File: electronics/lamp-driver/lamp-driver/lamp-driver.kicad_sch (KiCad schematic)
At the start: 30 parts, among them J1 Conn_01x04_Pin, J12V1 Conn_01x02_Pin, J2 Conn_01x04_Pin, J3 Conn_01x04_Pin, J4 Conn_01x04_Pin, J5 Conn_01x04_Pin, J6 Conn_01x04_Pin, Q1 AO3400A, U1 LM78M05_TO252

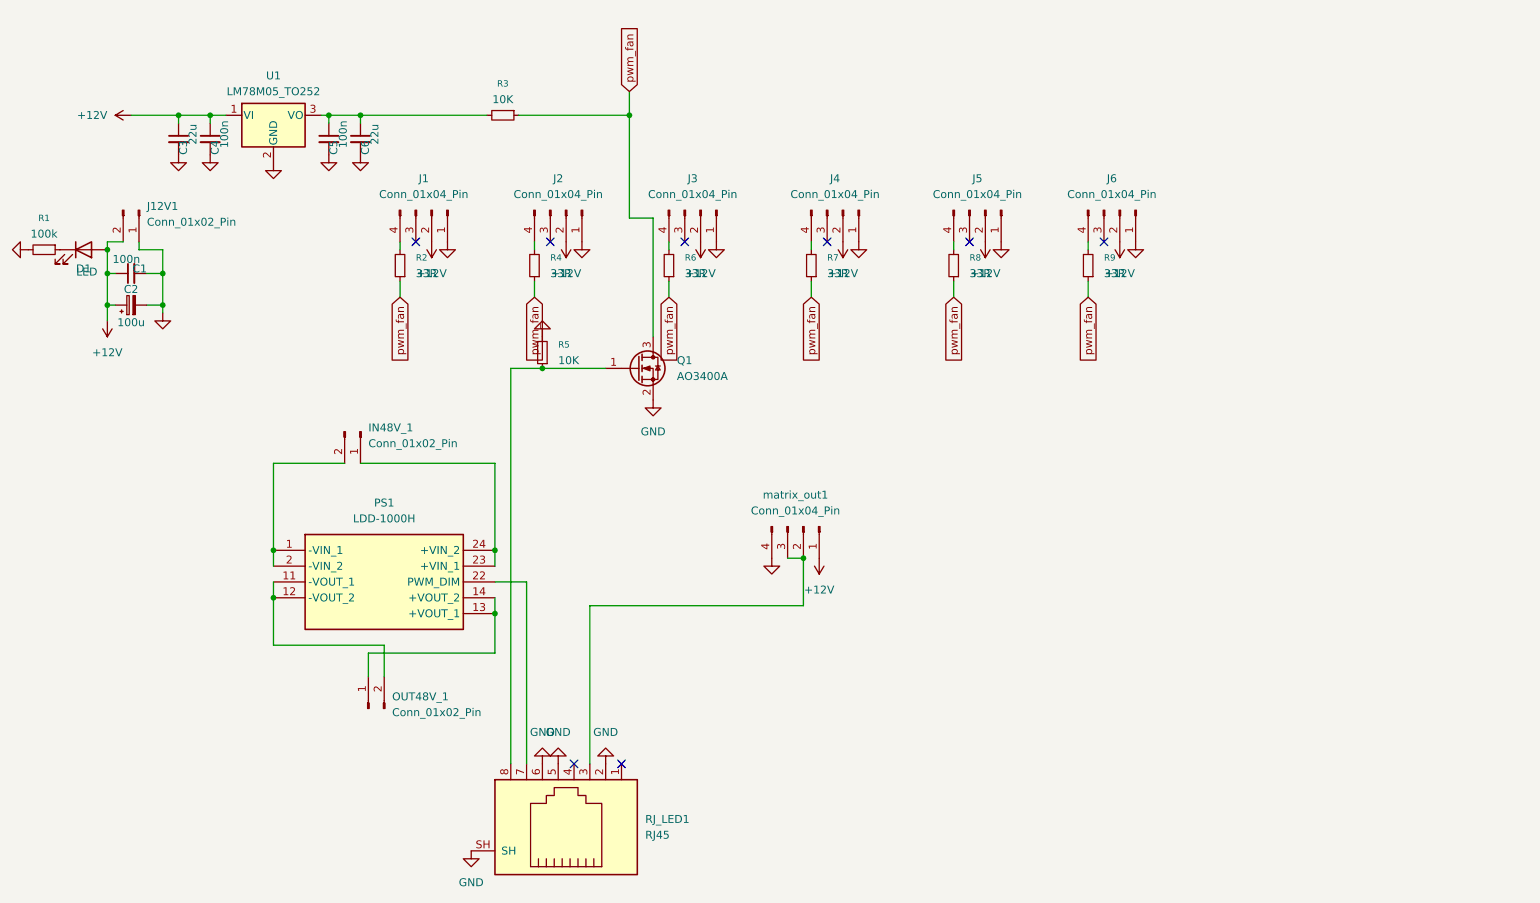
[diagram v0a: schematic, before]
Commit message: lamp fans control added; uv boost anims added; ambiente light timeout fixed
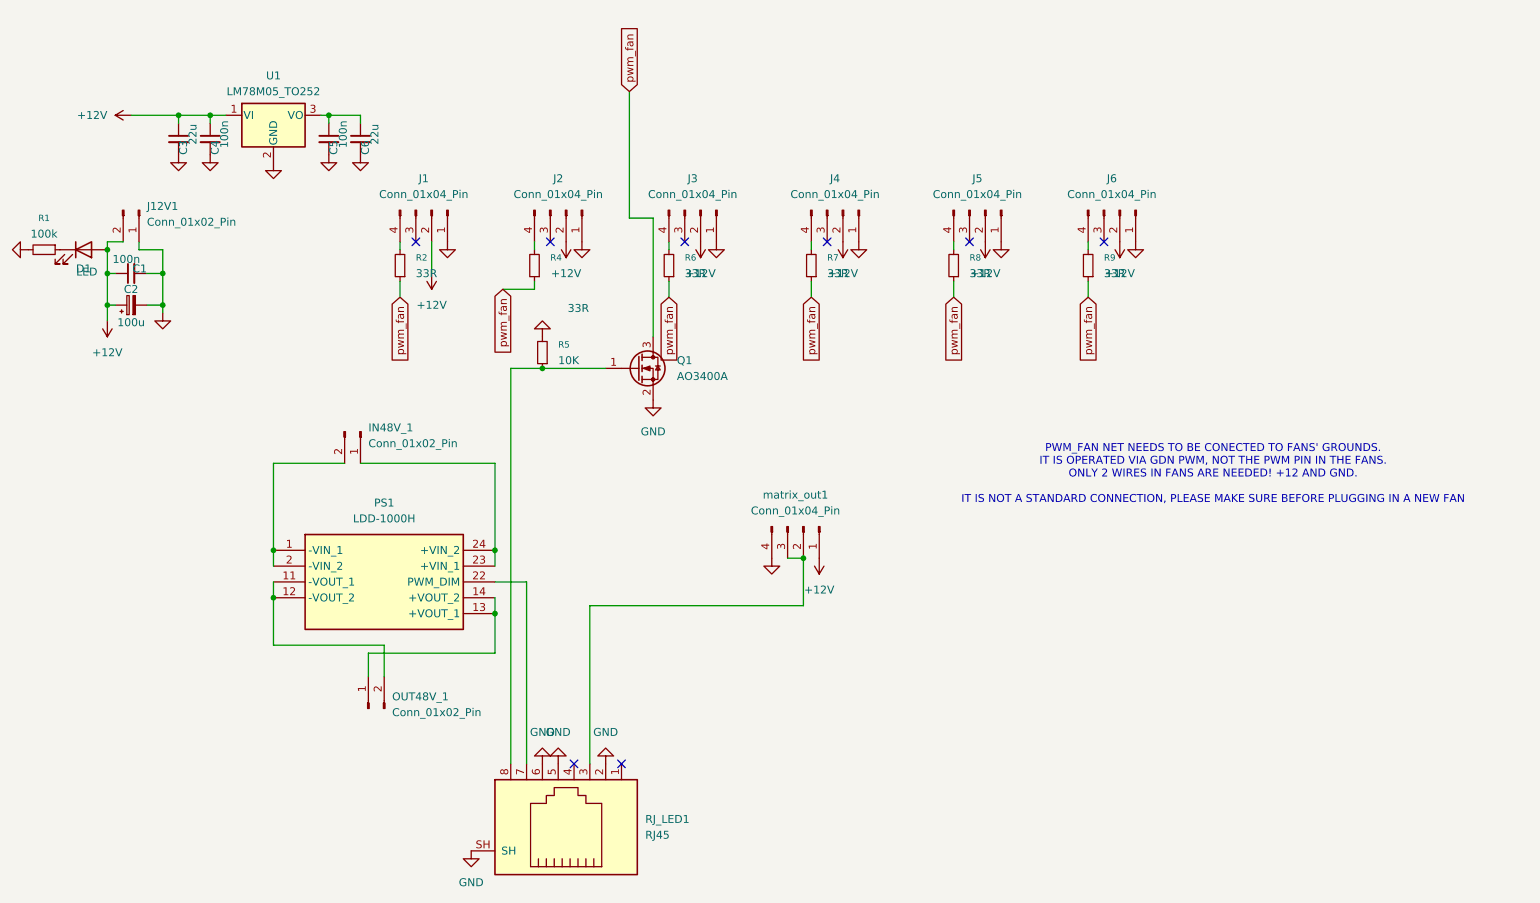
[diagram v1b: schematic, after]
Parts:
- removed R3: 10K, Resistor_SMD:R_0805_2012Metric, symbol Device:R_Small
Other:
- note added: "PWM_FAN NET NEEDS TO BE CONECTED TO FANS' GROUNDS. IT IS OPERATED VIA GDN PWM, NOT THE PWM PIN IN THE FANS. ONLY 2 WIRES IN FANS ARE NEEDED! +12 AND GND. IT IS NOT A STANDARD CONNECTION, PLEASE MAKE SURE BEFORE PLUGGING IN A NEW FAN"
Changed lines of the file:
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@@
 	(generator_version "9.0")
 	(paper "A4")
+	(text "PWM_FAN NET NEEDS TO BE CONECTED TO FANS' GROUNDS. \nIT IS OPERATED VIA GDN PWM, NOT THE PWM PIN IN THE FANS. \nONLY 2 WIRES IN FANS ARE NEEDED! +12 AND GND. \n\nIT IS NOT A STANDARD CONNECTION, PLEASE MAKE SURE BEFORE PLUGGING IN A NEW FAN"
+		(exclude_from_sim no)
+		(at 192.786 74.168 0)
+		(effects
+			(font
+				(size 1.27 1.27)
+			)
+		)
+	)
 	(junction
 		(at 127 87.63)
@@
 	)
 	(junction
-		(at 55.88 16.51)
-		(diameter 0)
-		(color 0 0 0 0)
-	)
-	(junction
 		(at 24.13 46.99)
 		(diameter 0)
@@
 	)
 	(junction
-		(at 99.06 16.51)
-		(diameter 0)
-		(color 0 0 0 0)
-	)
-	(junction
 		(at 24.13 41.91)
 		(diameter 0)
@@
 	(wire
 		(pts
+			(xy 83.82 44.45) (xy 83.82 43.18)
+		)
+		(stroke
+			(width 0)
+			(type default)
+		)
+	)
+	(wire
+		(pts
 			(xy 124.46 87.63) (xy 127 87.63)
 		)
@@
 	(wire
 		(pts
-			(xy 99.06 12.7) (xy 99.06 16.51)
+			(xy 99.06 12.7) (xy 99.06 33.02)
 		)
 		(stroke
@@
 	(wire
 		(pts
-			(xy 81.28 16.51) (xy 99.06 16.51)
+			(xy 128.27 45.72) (xy 128.27 43.18)
 		)
 		(stroke
@@
 	(wire
 		(pts
-			(xy 128.27 45.72) (xy 128.27 43.18)
+			(xy 127 95.25) (xy 127 87.63)
 		)
 		(stroke
@@
 	(wire
 		(pts
-			(xy 127 95.25) (xy 127 87.63)
+			(xy 85.09 57.15) (xy 95.25 57.15)
 		)
 		(stroke
@@
 	(wire
 		(pts
-			(xy 85.09 57.15) (xy 95.25 57.15)
+			(xy 77.47 93.98) (xy 77.47 96.52)
 		)
 		(stroke
@@
 	(wire
 		(pts
-			(xy 77.47 93.98) (xy 77.47 96.52)
+			(xy 151.13 38.1) (xy 151.13 36.83)
 		)
 		(stroke
@@
 	(wire
 		(pts
-			(xy 151.13 38.1) (xy 151.13 36.83)
+			(xy 67.31 41.91) (xy 67.31 36.83)
 		)
 		(stroke
@@
 	(wire
 		(pts
-			(xy 55.88 16.51) (xy 76.2 16.51)
-		)
-		(stroke
-			(width 0)
-			(type default)
-		)
-	)
-	(wire
-		(pts
 			(xy 82.55 91.44) (xy 82.55 120.65)
 		)
@@
 	(wire
 		(pts
-			(xy 99.06 16.51) (xy 99.06 33.02)
-		)
-		(stroke
-			(width 0)
-			(type default)
-		)
-	)
-	(wire
-		(pts
 			(xy 105.41 38.1) (xy 105.41 36.83)
 		)
@@
 	(wire
 		(pts
-			(xy 92.71 95.25) (xy 127 95.25)
+			(xy 78.74 44.45) (xy 83.82 44.45)
 		)
 		(stroke
@@
 	(wire
 		(pts
-			(xy 41.91 101.6) (xy 59.69 101.6)
+			(xy 92.71 95.25) (xy 127 95.25)
 		)
 		(stroke
@@
 	(wire
 		(pts
-			(xy 83.82 45.72) (xy 83.82 43.18)
+			(xy 41.91 101.6) (xy 59.69 101.6)
 		)
 		(stroke
@@
 	(global_label "pwm_fan"
 		(shape input)
-		(at 83.82 45.72 270)
+		(at 78.74 44.45 270)
 		(fields_autoplaced yes)
 		(effects
@@
 		)
 		(property "Intersheetrefs" "${INTERSHEET_REFS}"
-			(at 83.82 56.8693 90)
+			(at 78.74 55.5993 90)
 			(effects
 				(font
@@
 		(on_board yes)
 		(dnp no)
-		(fields_autoplaced yes)
 		(property "Reference" "R4"
 			(at 86.36 39.3699 0)
@@
 		)
 		(property "Value" "33R"
-			(at 86.36 41.9099 0)
+			(at 89.154 47.498 0)
 			(effects
 				(font
@@
 	(symbol
 		(lib_id "power:+12V")
-		(at 67.31 36.83 180)
+		(at 67.31 41.91 180)
 		(unit 1)
 		(exclude_from_sim no)
@@
 		(fields_autoplaced yes)
 		(property "Reference" "#PWR010"
-			(at 67.31 33.02 0)
+			(at 67.31 38.1 0)
 			(effects
 				(font
@@
 		)
 		(property "Value" "+12V"
-			(at 67.31 41.91 0)
+			(at 67.31 46.99 0)
 			(effects
 				(font
@@
 		)
 		(property "Footprint" ""
-			(at 67.31 36.83 0)
+			(at 67.31 41.91 0)
 			(effects
 				(font
@@
 		)
 		(property "Datasheet" ""
-			(at 67.31 36.83 0)
+			(at 67.31 41.91 0)
 			(effects
 				(font
@@
 		)
 		(property "Description" "Power symbol creates a global label with name \"+12V\""
-			(at 67.31 36.83 0)
+			(at 67.31 41.91 0)
 			(effects
 				(font
@@
 					(unit 1)
 				)
-			)
-		)
-	)
-	(symbol
-		(lib_id "Device:R_Small")
-		(at 78.74 16.51 270)
-		(unit 1)
-		(exclude_from_sim no)
-		(in_bom yes)
-		(on_board yes)
-		(dnp no)
-		(fields_autoplaced yes)
-		(property "Reference" "R3"
-			(at 78.74 11.43 90)
-			(effects
-				(font
-					(size 1.016 1.016)
-				)
-			)
-		)
-		(property "Value" "10K"
-			(at 78.74 13.97 90)
-			(effects
-				(font
-					(size 1.27 1.27)
-				)
-			)
-		)
-		(property "Footprint" "Resistor_SMD:R_0805_2012Metric"
-			(at 78.74 16.51 0)
-			(effects
-				(font
-					(size 1.27 1.27)
-				)
-				(hide yes)
-			)
-		)
-		(property "Datasheet" "~"
-			(at 78.74 16.51 0)
-			(effects
-				(font
-					(size 1.27 1.27)
-				)
-				(hide yes)
-			)
-		)
-		(property "Description" "Resistor, small symbol"
-			(at 78.74 16.51 0)
-			(effects
-				(font
-					(size 1.27 1.27)
-				)
-				(hide yes)
-			)
-		)
-		(pin "2"
-		)
-		(pin "1"
-		)
-		(instances
-			(project "lamp-driver"
-				(path "/8d1b4815-1b67-41e7-a6f2-54ca5c4f4dfa"
-					(reference "R3")
-					(unit 1)
-				)

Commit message: fail safe added to lamp fans
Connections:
- net GND: no longer R5.2
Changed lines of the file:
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@@
-	)
-	(symbol
-		(lib_id "power:GND")
-		(at 85.09 52.07 180)
-		(unit 1)
-		(exclude_from_sim no)
-		(in_bom yes)
-		(on_board yes)
-		(dnp no)
-		(fields_autoplaced yes)
-		(property "Reference" "#PWR012"
-			(at 85.09 45.72 0)
-			(effects
-				(font
-					(size 1.27 1.27)
-				)
-				(hide yes)
-			)
-		)
-		(property "Value" "GND"
-			(at 85.09 46.99 0)
-			(effects
-				(font
-					(size 1.27 1.27)
-				)
-				(hide yes)
-			)
-		)
-		(property "Footprint" ""
-			(at 85.09 52.07 0)
-			(effects
-				(font
-					(size 1.27 1.27)
-				)
-				(hide yes)
-			)
-		)
-		(property "Datasheet" ""
-			(at 85.09 52.07 0)
-			(effects
-				(font
-					(size 1.27 1.27)
-				)
-				(hide yes)
-			)
-		)
-		(property "Description" "Power symbol creates a global label with name \"GND\" , ground"
-			(at 85.09 52.07 0)
-			(effects
-				(font
-					(size 1.27 1.27)
-				)
-				(hide yes)
-			)
-		)
-		(pin "1"
-		)
-		(instances
-			(project "lamp-driver"
-				(path "/8d1b4815-1b67-41e7-a6f2-54ca5c4f4dfa"
-					(reference "#PWR012")
-					(unit 1)
-				)
-			)
-		)
 	)
 	(symbol

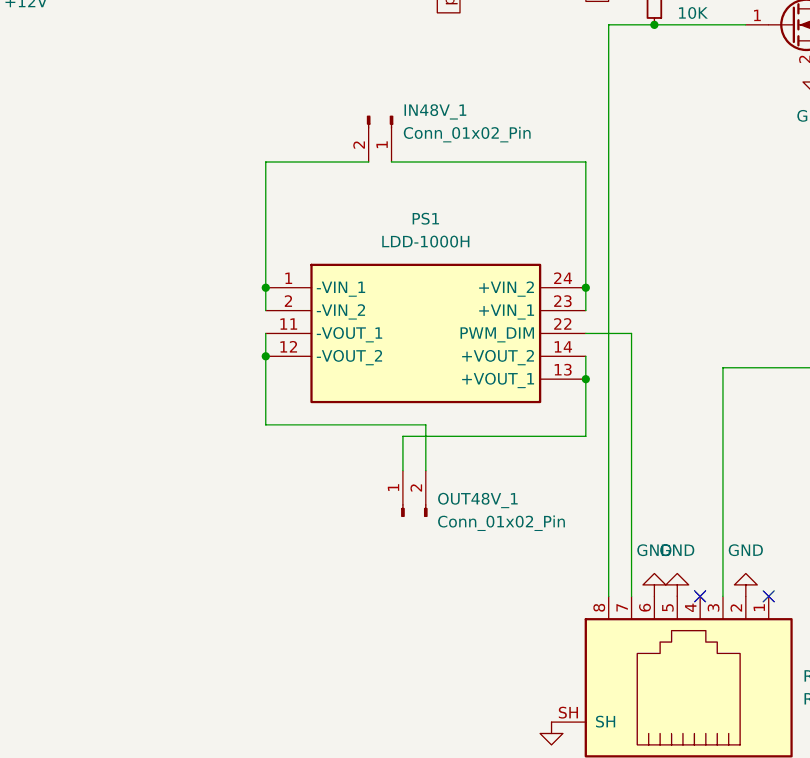
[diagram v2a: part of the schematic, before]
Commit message: UV control fixed
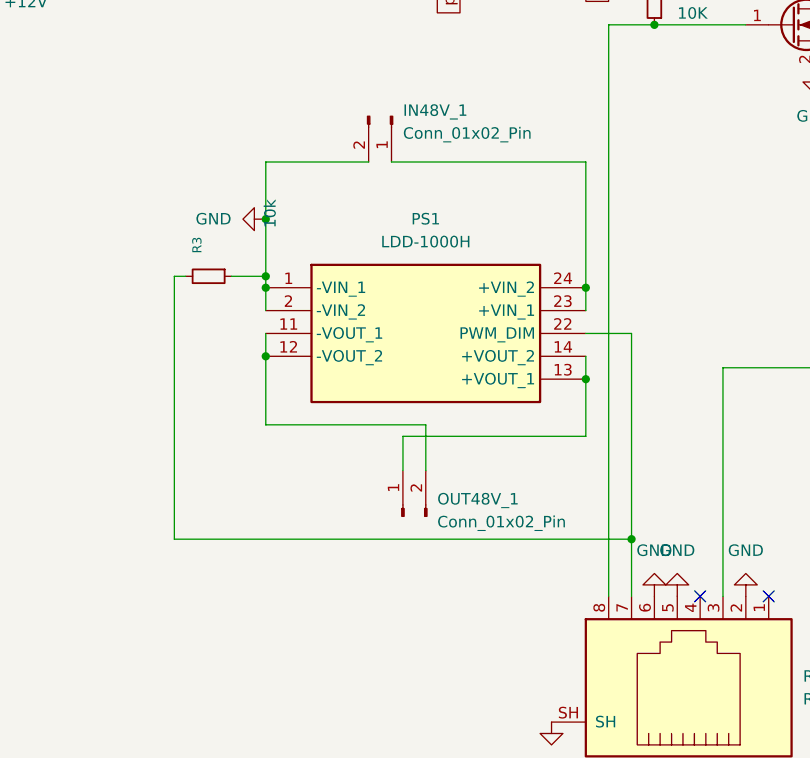
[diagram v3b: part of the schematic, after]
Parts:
- added R3: 10k, Resistor_SMD:R_0805_2012Metric, symbol Device:R_Small
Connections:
- net GND: now also IN48V_1.2 (Pin_2), PS1.1 (-VIN_1), PS1.2 (-VIN_2), R3.1
- net at PS1.22 (PWM_DIM), RJ_LED1.7: now also R3.2
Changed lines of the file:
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@@
 	)
 	(junction
+		(at 41.91 78.74)
+		(diameter 0)
+		(color 0 0 0 0)
+	)
+	(junction
 		(at 15.24 38.1)
 		(diameter 0)
@@
 	)
 	(junction
+		(at 82.55 114.3)
+		(diameter 0)
+		(color 0 0 0 0)
+	)
+	(junction
+		(at 41.91 85.09)
+		(diameter 0)
+		(color 0 0 0 0)
+	)
+	(junction
 		(at 24.13 41.91)
 		(diameter 0)
@@
 	(wire
 		(pts
-			(xy 41.91 72.39) (xy 41.91 86.36)
+			(xy 41.91 72.39) (xy 41.91 78.74)
 		)
 		(stroke
@@
 	(wire
 		(pts
+			(xy 41.91 85.09) (xy 41.91 86.36)
+		)
+		(stroke
+			(width 0)
+			(type default)
+		)
+	)
+	(wire
+		(pts
 			(xy 99.06 12.7) (xy 99.06 33.02)
 		)
@@
 	(wire
 		(pts
+			(xy 31.75 85.09) (xy 33.02 85.09)
+		)
+		(stroke
+			(width 0)
+			(type default)
+		)
+	)
+	(wire
+		(pts
 			(xy 77.47 96.52) (xy 77.47 102.87)
 		)
@@
 	(wire
 		(pts
+			(xy 41.91 78.74) (xy 41.91 85.09)
+		)
+		(stroke
+			(width 0)
+			(type default)
+		)
+	)
+	(wire
+		(pts
 			(xy 128.27 45.72) (xy 128.27 43.18)
 		)
@@
 	(wire
 		(pts
+			(xy 82.55 114.3) (xy 82.55 120.65)
+		)
+		(stroke
+			(width 0)
+			(type default)
+		)
+	)
+	(wire
+		(pts
+			(xy 82.55 114.3) (xy 31.75 114.3)
+		)
+		(stroke
+			(width 0)
+			(type default)
+		)
+	)
+	(wire
+		(pts
 			(xy 55.88 72.39) (xy 77.47 72.39)
 		)
@@
 	(wire
 		(pts
-			(xy 82.55 91.44) (xy 82.55 120.65)
+			(xy 82.55 91.44) (xy 82.55 114.3)
 		)
 		(stroke
@@
 	(wire
 		(pts
+			(xy 31.75 85.09) (xy 31.75 114.3)
+		)
+		(stroke
+			(width 0)
+			(type default)
+		)
+	)
+	(wire
+		(pts
 			(xy 80.01 120.65) (xy 80.01 57.15)
 		)
@@
 	(wire
 		(pts
+			(xy 38.1 85.09) (xy 41.91 85.09)
+		)
+		(stroke
+			(width 0)
+			(type default)
+		)
+	)
+	(wire
+		(pts
 			(xy 41.91 101.6) (xy 59.69 101.6)
 		)
@@
 	)
 	(symbol
+		(lib_id "Device:R_Small")
+		(at 35.56 85.09 270)
+		(unit 1)
+		(exclude_from_sim no)
+		(in_bom yes)
+		(on_board yes)
+		(dnp no)
+		(property "Reference" "R3"
+			(at 34.2899 82.55 0)
+			(effects
+				(font
+					(size 1.016 1.016)
+				)
+				(justify right)
+			)
+		)
+		(property "Value" "10k"
+			(at 42.418 79.756 0)
+			(effects
+				(font
+					(size 1.27 1.27)
+				)
+				(justify right)
+			)
+		)
+		(property "Footprint" "Resistor_SMD:R_0805_2012Metric"
+			(at 35.56 85.09 0)
+			(effects
+				(font
+					(size 1.27 1.27)
+				)
+				(hide yes)
+			)
+		)
+		(property "Datasheet" "~"
+			(at 35.56 85.09 0)
+			(effects
+				(font
+					(size 1.27 1.27)
+				)
+				(hide yes)
+			)
+		)
+		(property "Description" "Resistor, small symbol"
+			(at 35.56 85.09 0)
+			(effects
+				(font
+					(size 1.27 1.27)
+				)
+				(hide yes)
+			)
+		)
+		(pin "2"
+		)
+		(pin "1"
+		)
+		(instances
+			(project "lamp-driver"
+				(path "/8d1b4815-1b67-41e7-a6f2-54ca5c4f4dfa"
+					(reference "R3")
+					(unit 1)
+				)
+			)
+		)
+	)
+	(symbol
 		(lib_id "Connector:Conn_01x04_Pin")
 		(at 127 82.55 270)
@@
 					(unit 1)
 				)
+			)
+		)
+	)
+	(symbol
+		(lib_id "power:GND")
+		(at 41.91 78.74 270)
+		(unit 1)
+		(exclude_from_sim no)
+		(in_bom yes)
+		(on_board yes)
+		(dnp no)
+		(fields_autoplaced yes)
+		(property "Reference" "#PWR012"
+			(at 35.56 78.74 0)
+			(effects
+				(font
+					(size 1.27 1.27)
+				)
+				(hide yes)
+			)
+		)
+		(property "Value" "GND"
+			(at 38.1 78.7399 90)
+			(effects
+				(font
+					(size 1.27 1.27)
+				)
+				(justify right)
+			)
+		)
+		(property "Footprint" ""
+			(at 41.91 78.74 0)
+			(effects
+				(font
+					(size 1.27 1.27)
+				)
+				(hide yes)
+			)
+		)
+		(property "Datasheet" ""
+			(at 41.91 78.74 0)
+			(effects
+				(font
+					(size 1.27 1.27)
+				)
+				(hide yes)
+			)
+		)
+		(property "Description" "Power symbol creates a global label with name \"GND\" , ground"
+			(at 41.91 78.74 0)
+			(effects
+				(font
+					(size 1.27 1.27)
+				)
+				(hide yes)
+			)
+		)
+		(pin "1"
+		)
+		(instances
+			(project "lamp-driver"
+				(path "/8d1b4815-1b67-41e7-a6f2-54ca5c4f4dfa"
+					(reference "#PWR012")
+					(unit 1)
+				)

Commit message: uv control fixed
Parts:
- removed R2, R4, R6, R7, R8, R9: 33R, Resistor_SMD:R_0805_2012Metric, symbol Device:R_Small
- removed R5: 10K, Resistor_SMD:R_0805_2012Metric, symbol Device:R_Small
- added D2, D3, D8: D_Schottky_SS14, Diode_SMD:D_SMA, symbol Device:D_Schottky
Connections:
- net +12V: now also D2.1 (K), D3.1 (K), D8.1 (K)
- net GND: no longer J1.1 (Pin_1), J2.1 (Pin_1), J3.1 (Pin_1), J4.1 (Pin_1), J5.1 (Pin_1), J6.1 (Pin_1)
- net pwm_fan: now also J1.1 (Pin_1), J2.1 (Pin_1), J3.1 (Pin_1), J4.1 (Pin_1), J5.1 (Pin_1), J6.1 (Pin_1), D2.2 (A), D3.2 (A), D8.2 (A)
- no-connect marks 8 -> 14
